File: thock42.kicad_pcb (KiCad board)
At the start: 2 copper layers, 132 x 99.6 mm, 78 parts, among them J1 OLED-128x32, SW1 SW_Push, SW10 SW_Push, SW11 SW_Push, SW12 SW_Push, SW13 SW_Push, SW14 SW_Push, SW15 SW_Push, SW16 SW_Push, SW17 SW_Push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

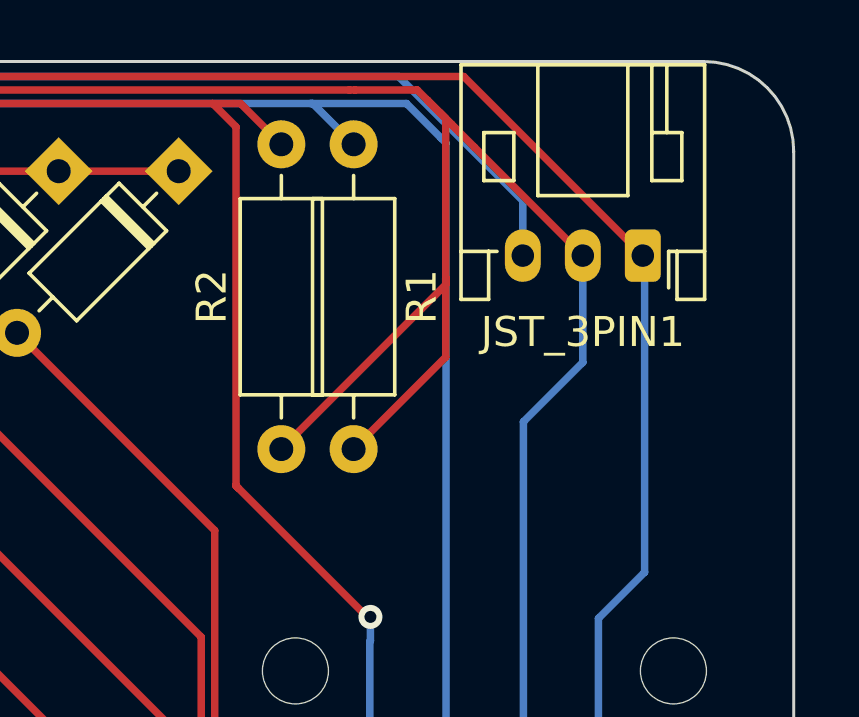
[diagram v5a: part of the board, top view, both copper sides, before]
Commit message: add space between resistors and change some silkscreen labels
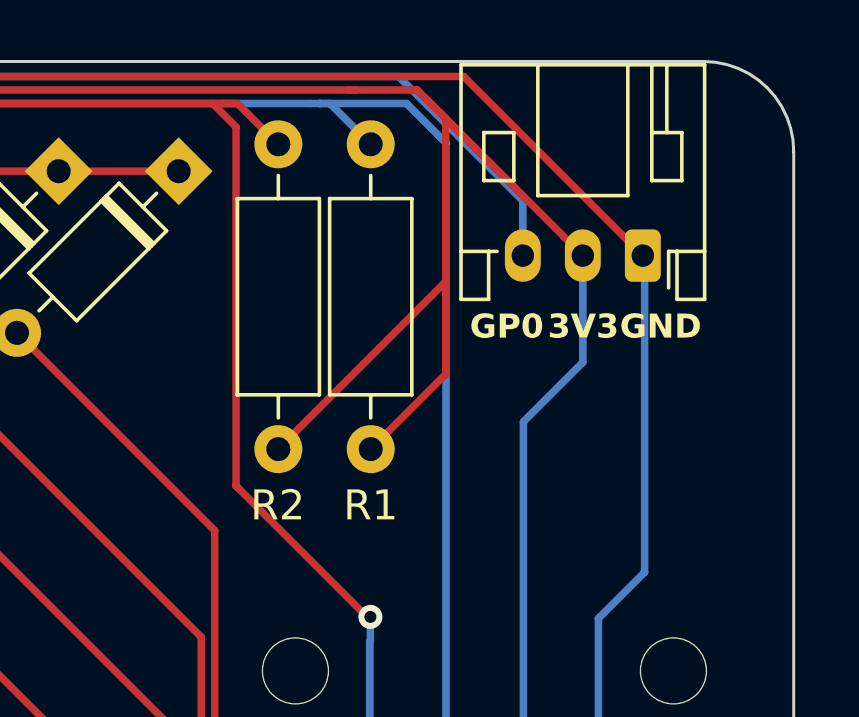
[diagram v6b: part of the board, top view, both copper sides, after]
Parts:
- moved R1 0.57 mm to (203.9, 50.8)
- moved R2 0.10 mm to (200.8, 50.8)
- renumbered JST_3PIN1 to JST_3PIN
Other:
- board text added: "GP0"
- board text removed: "JST_3PIN1"
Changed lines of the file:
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@@
 	(footprint "Resistor_THT:R_Axial_DIN0207_L6.3mm_D2.5mm_P10.16mm_Horizontal"
 		(layer "F.Cu")
-		(at 203.33 50.76 -90)
+		(at 203.9 50.76 -90)
 		(descr "Resistor, Axial_DIN0207 series, Axial, Horizontal, pin pitch=10.16mm, 0.25W = 1/4W, length*diameter=6.3*2.5mm^2, http://cdn-reichelt.de/documents/datenblatt/B400/1_4W%23YAG.pdf")
 		(tags "Resistor Axial_DIN0207 series Axial Horizontal pin pitch 10.16mm 0.25W = 1/4W length 6.3mm diameter 2.5mm")
 		(property "Reference" "R1"
-			(at 5.08 -2.27 -90)
+			(at 12.04 0 0)
 			(layer "F.SilkS")
 			(effects
@@
 		(descr "JST PH series connector, S3B-PH-K (http://www.jst-mfg.com/product/pdf/eng/ePH.pdf), generated with kicad-footprint-generator")
 		(tags "connector JST PH top entry")
-		(property "Reference" "JST_3PIN1"
+		(property "Reference" "JST_3PIN"
 			(at 2 -2.55 180)
 			(layer "F.SilkS")
+			(hide yes)
 			(effects
 				(font
@@
 	(footprint "Resistor_THT:R_Axial_DIN0207_L6.3mm_D2.5mm_P10.16mm_Horizontal"
 		(layer "F.Cu")
-		(at 200.92 50.76 -90)
+		(at 200.82 50.76 -90)
 		(descr "Resistor, Axial_DIN0207 series, Axial, Horizontal, pin pitch=10.16mm, 0.25W = 1/4W, length*diameter=6.3*2.5mm^2, http://cdn-reichelt.de/documents/datenblatt/B400/1_4W%23YAG.pdf")
 		(tags "Resistor Axial_DIN0207 series Axial Horizontal pin pitch 10.16mm 0.25W = 1/4W length 6.3mm diameter 2.5mm")
 		(property "Reference" "R2"
-			(at 5.08 2.32 -90)
+			(at 12.04 0.02 0)
 			(layer "F.SilkS")
 			(effects
@@
 		)
 	)
-	(gr_text "JST_3PIN1"
-		(at 214.83 57.6 -0)
-		(layer "B.SilkS")
-		(effects
-			(font
-				(size 1 1)
-				(thickness 0.15)
-			)
-			(justify left bottom mirror)
-		)
-	)
 	(gr_text "D4"
 		(at 147.8 58.2 45)
@@
 		)
 	)
+	(gr_text "GP0"
+		(at 209.7 57.3 0)
+		(layer "B.SilkS")
+		(effects
+			(font
+				(size 0.8 0.8)
+				(thickness 0.175)
+				(bold yes)
+			)
+			(justify left bottom mirror)
+		)
+	)
 	(gr_text "42"
 		(at 129.91 123 -0)
@@
 		)
 	)
+	(gr_text "GND"
+		(at 214.8 57.3 -0)
+		(layer "B.SilkS")
+		(effects
+			(font
+				(size 0.8 0.8)
+				(thickness 0.175)
+				(bold yes)
+			)
+			(justify left bottom mirror)
+		)
+	)
 	(gr_text "D13"
 		(at 119.6 58.4 45)
@@
 		)
 	)
+	(gr_text "3V3"
+		(at 212.1 57.3 -0)
+		(layer "B.SilkS")
+		(effects
+			(font
+				(size 0.8 0.8)
+				(thickness 0.175)
+				(bold yes)
+			)
+			(justify left bottom mirror)
+		)
+	)
 	(gr_text "D21"
 		(at 191.8 58.2 45)
@@
 		)
 	)
+	(gr_text "3V3"
+		(at 209.8 57.3 0)
+		(layer "F.SilkS")
+		(effects
+			(font
+				(size 0.8 0.8)
+				(thickness 0.175)
+				(bold yes)
+			)
+			(justify left bottom)
+		)
+	)
+	(gr_text "GP0"
+		(at 207.2 57.3 0)
+		(layer "F.SilkS")
+		(effects
+			(font
+				(size 0.8 0.8)
+				(thickness 0.175)
+				(bold yes)
+			)
+			(justify left bottom)
+		)
+	)
 	(gr_text "TH"
 		(at 130.65 125.42 0)
@@
 		)
 	)
+	(gr_text "GND"
+		(at 212.2 57.3 0)
+		(layer "F.SilkS")
+		(effects
+			(font
+				(size 0.8 0.8)
+				(thickness 0.175)
+				(bold yes)
+			)
+			(justify left bottom)
+		)
+	)
 	(gr_text "42"
 		(at 152.66 123 0)
@@
 	)
 	(segment
-		(start 201.97 49.4)
-		(end 201.9 49.4)
-		(width 0.25)
-		(layer "B.Cu")
-		(net 22)
-	)
-	(segment
 		(start 113.874193 50.257017)
 		(end 113.874193 52.325807)
@@
 	)
 	(segment
-		(start 205.093604 49.4)
-		(end 201.9 49.4)
-		(width 0.25)
-		(layer "B.Cu")
-		(net 22)
-	)
-	(segment
-		(start 203.33 50.76)
-		(end 201.97 49.4)
+		(start 202.54 49.4)
+		(end 202.2 49.4)
 		(width 0.25)
 		(layer "B.Cu")
@@
 	)
 	(segment
+		(start 202.2 49.4)
+		(end 201.9 49.4)
+		(width 0.25)
+		(layer "B.Cu")
+		(net 22)
+	)
+	(segment
 		(start 113.874193 52.325807)
 		(end 109.945 56.255)
@@
 	)
 	(segment
+		(start 205.093604 49.4)
+		(end 202.2 49.4)
+		(width 0.25)
+		(layer "B.Cu")
+		(net 22)
+	)
+	(segment
+		(start 203.9 50.76)
+		(end 202.54 49.4)
+		(width 0.25)
+		(layer "B.Cu")
+		(net 22)
+	)
+	(segment
 		(start 113.705904 49.4)
 		(end 113.431739 49.674165)
@@
 	)
 	(segment
-		(start 115.7 49.4)
-		(end 114.73121 49.4)
+		(start 198.63 49.4)
+		(end 199 49.4)
 		(width 0.25)
 		(layer "F.Cu")
@@
 	)
 	(segment
-		(start 199.56 49.4)
-		(end 199.32 49.4)
+		(start 115.7 49.4)
+		(end 114.73121 49.4)
 		(width 0.25)
 		(layer "F.Cu")
@@
 	)
 	(segment
+		(start 199 49.4)
+		(end 199.32 49.4)
+		(width 0.25)
+		(layer "F.Cu")
+		(net 23)
+	)
+	(segment
 		(start 211.49 107.162604)
 		(end 205.19 100.862604)
@@
 	)
 	(segment
-		(start 198.63 49.4)
-		(end 199.32 49.4)
+		(start 200.82 50.76)
+		(end 199.46 49.4)
 		(width 0.25)
 		(layer "F.Cu")
@@
 	)
 	(segment
-		(start 205.19 100.862604)
-		(end 205.19 100.813604)
+		(start 199.46 49.4)
+		(end 199 49.4)
 		(width 0.25)
 		(layer "F.Cu")
@@
 	)
 	(segment
-		(start 200.92 50.76)
-		(end 199.56 49.4)
+		(start 205.19 100.862604)
+		(end 205.19 100.813604)
 		(width 0.25)
 		(layer "F.Cu")
@@
 	)
 	(segment
-		(start 200.92 60.92)
-		(end 206.4 55.44)
-		(width 0.25)
-		(layer "F.Cu")
-		(net 25)
-	)
-	(segment
-		(start 206.4 57.85)
-		(end 206.4 55.2)
-		(width 0.25)
-		(layer "F.Cu")
-		(net 25)
-	)
-	(segment
 		(start 207.245091 106.327513)
 		(end 209.723909 106.327513)
@@
 	)
 	(segment
-		(start 203.33 60.92)
-		(end 206.4 57.85)
+		(start 201.49 108.113604)
+		(end 201.49 94.513604)
 		(width 0.25)
 		(layer "F.Cu")
@@
 	)
 	(segment
-		(start 206.4 49.9)
-		(end 205.8 49.3)
+		(start 104.231 53.715)
+		(end 103.176 54.77)
 		(width 0.25)
 		(layer "F.Cu")
@@
 	)
 	(segment
-		(start 201.49 108.113604)
-		(end 201.49 94.513604)
+		(start 206.4 54.8)
+		(end 206.4 49.9)
 		(width 0.25)
 		(layer "F.Cu")
@@
 	)
 	(segment
-		(start 104.231 53.715)
-		(end 103.176 54.77)
+		(start 206.4 49.9)
+		(end 205.8 49.3)
 		(width 0.25)
 		(layer "F.Cu")
@@
 	)
 	(segment
+		(start 206.4 58.42)
+		(end 206.4 54.8)
+		(width 0.25)
+		(layer "F.Cu")
+		(net 25)
+	)
+	(segment
 		(start 205.8 49.3)
 		(end 205.45 48.95)
@@
 	)
 	(segment
-		(start 206.4 55.2)
-		(end 206.4 49.9)
-		(width 0.25)
-		(layer "F.Cu")
-		(net 25)
-	)
-	(segment
 		(start 203.19 48.95)
 		(end 110.186396 48.95)
@@
 	)
 	(segment
-		(start 206.4 55.44)
-		(end 206.4 55.2)
+		(start 205.45 48.95)
+		(end 203.38 48.95)
 		(width 0.25)
 		(layer "F.Cu")
@@
 	)
 	(segment
-		(start 205.45 48.95)
-		(end 203.38 48.95)
+		(start 200.82 60.92)
+		(end 206.4 55.34)
 		(width 0.25)
 		(layer "F.Cu")
@@
 	)
 	(segment
+		(start 203.9 60.92)
+		(end 206.4 58.42)
+		(width 0.25)
+		(layer "F.Cu")
+		(net 25)
+	)
+	(segment
 		(start 202.59 110.513604)
 		(end 201.49 109.413604)
@@
 		(width 0.25)
 		(layer "F.Cu")
+		(net 25)
+	)
+	(segment
+		(start 206.4 55.34)
+		(end 206.4 54.8)
+		(width 0.25)
+		(layer "F.Cu")

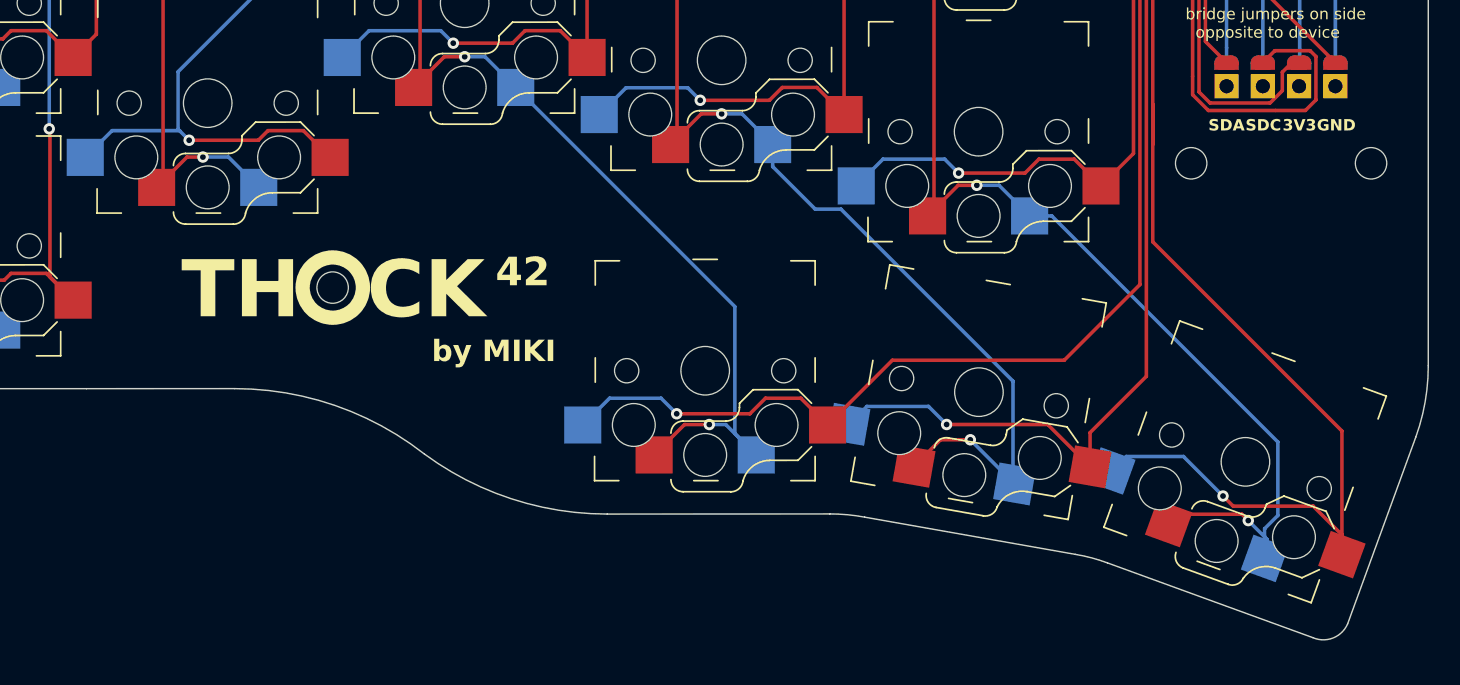
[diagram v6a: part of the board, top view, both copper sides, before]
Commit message: moev thumb cluster down by .2mm
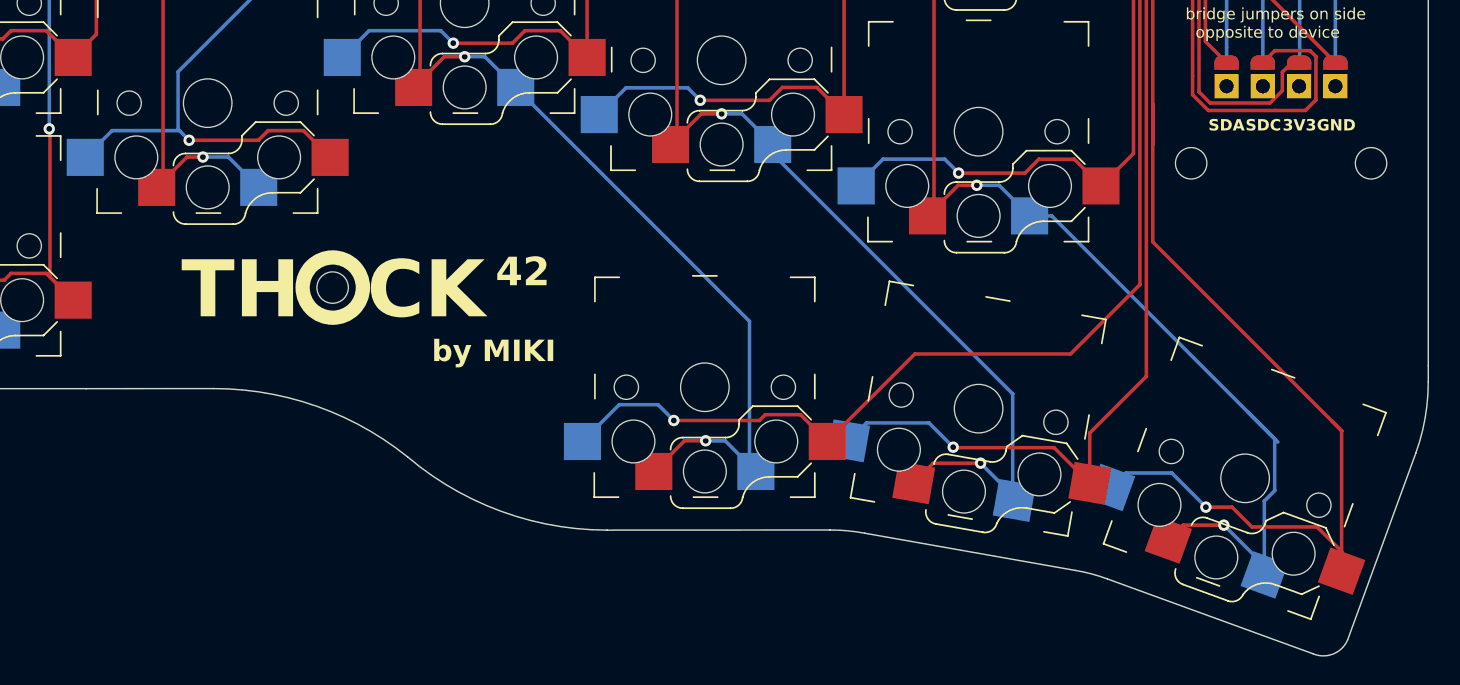
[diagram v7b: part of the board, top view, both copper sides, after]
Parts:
- moved SW19 1.16 mm to (167.3, 129.9)
- moved SW20 1.16 mm to (186.5, 131.4)
- moved SW21 1.16 mm to (205.2, 136.3)
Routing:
- net COL5: track 208.4 -> 212.0 mm
- net Net-(D21-A): track 115.8 -> 118.0 mm
- net Net-(D20-A): track 103.4 -> 104.6 mm
- net COL3: track 157.1 -> 158.2 mm
- net Net-(D19-A): track 116.9 -> 117.4 mm
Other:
- board size 132 x 99.6 mm -> 132 x 100.7 mm

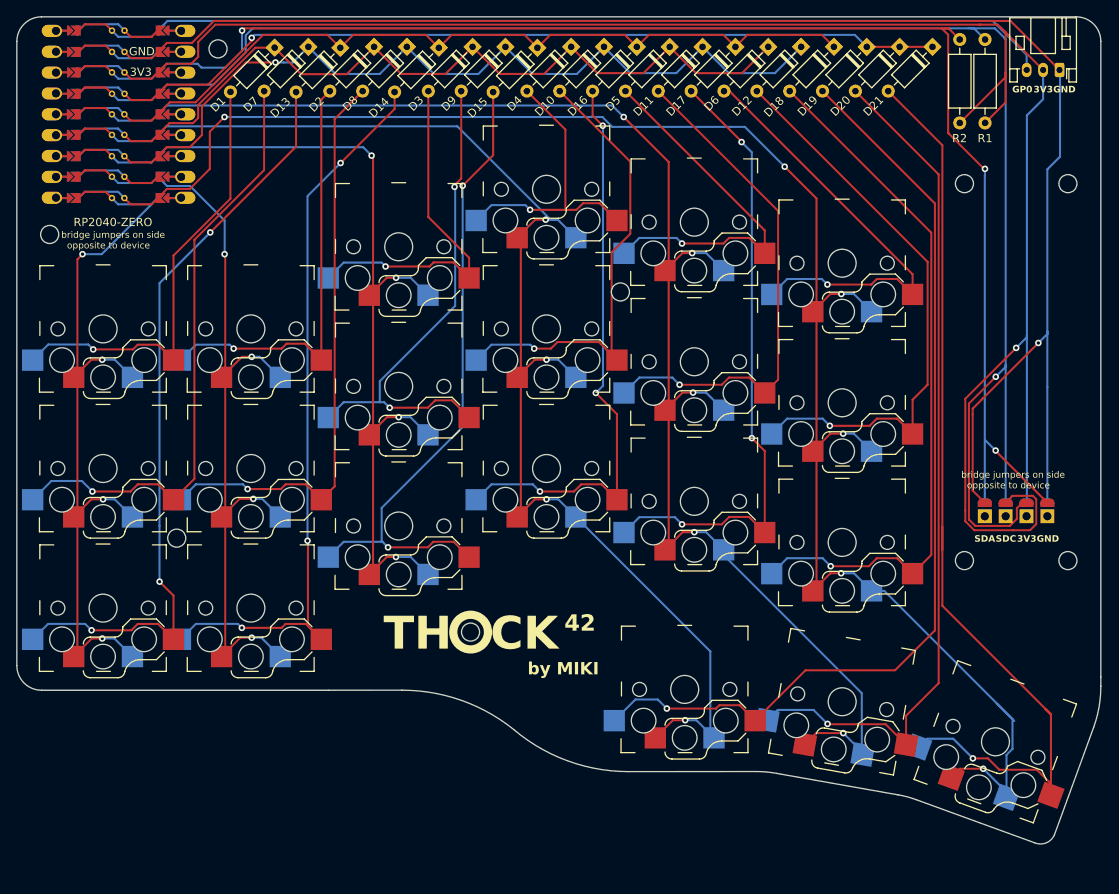
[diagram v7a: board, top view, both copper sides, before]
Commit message: adapt to symmetric keycap spacing
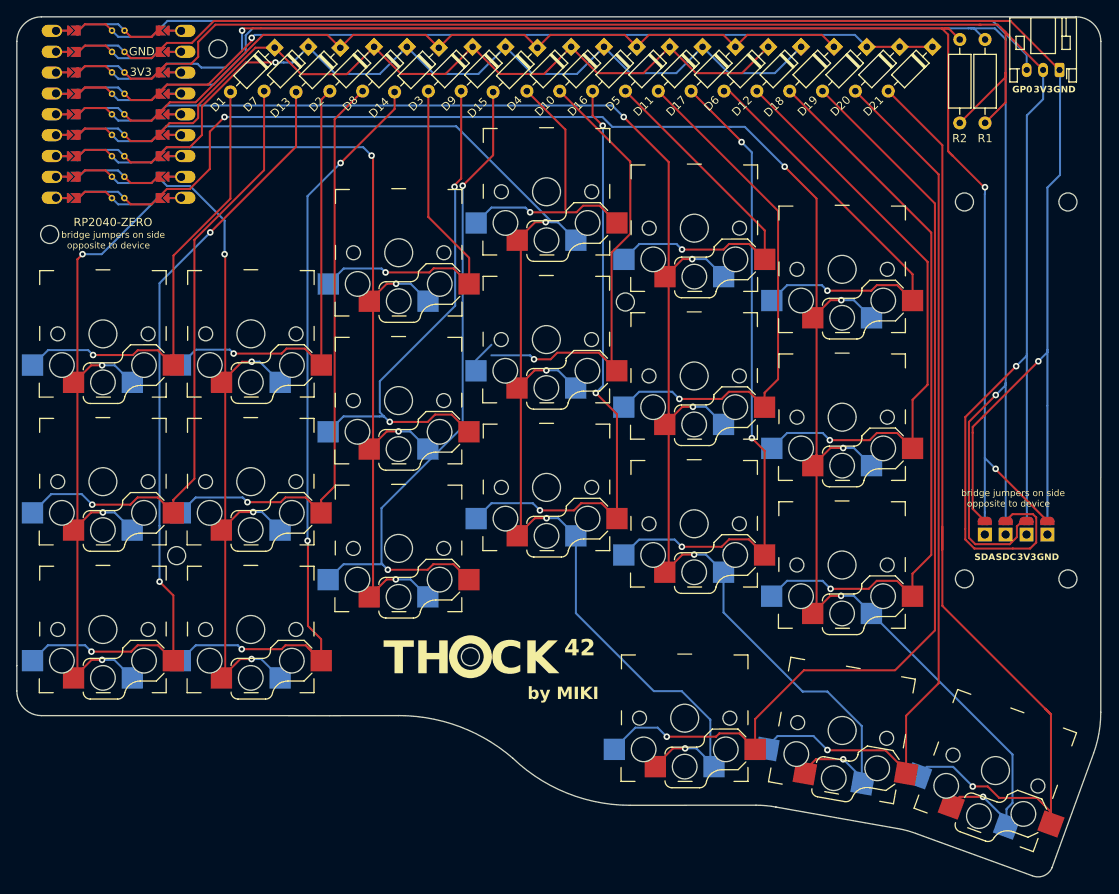
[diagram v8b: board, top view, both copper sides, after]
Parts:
- moved SW19 3.50 mm to (167.3, 133.4)
- moved SW20 3.50 mm to (186.5, 134.9)
- moved SW21 3.50 mm to (205.2, 139.8)
- moved REF** 3.00 mm to (141.2, 125.9)
- moved SW18 2.75 mm to (186.5, 114.8)
- moved SW15 2.73 mm to (132.5, 112.7)
- moved SW17 2.73 mm to (168.5, 109.7)
- moved SW13 2.60 mm to (96.5, 122.6)
- moved SW14 2.60 mm to (114.5, 122.6)
- moved SW16 2.30 mm to (150.5, 105.3)
- moved REF** 2.23 mm to (201.4, 70.5)
- moved REF** 2.23 mm to (214.0, 70.5)
- moved J1 2.23 mm to (201.7, 112.6)
- moved REF** 2.23 mm to (214.0, 116.4)
- moved REF** 2.23 mm to (201.4, 116.4)
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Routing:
- net COL4: track 181.2 -> 188.3 mm
- net COL3: track 158.2 -> 164.5 mm
- net Net-(D14-A): track 90.8 -> 95.7 mm
- net COL2: track 105.7 -> 109.6 mm
- net Net-(D19-A): track 117.4 -> 121.0 mm
- net COL1: track 91.7 -> 95.2 mm
- net COL0: track 89.0 -> 92.6 mm
- net Net-(D21-A): track 118.0 -> 121.4 mm
- net Net-(D20-A): track 104.6 -> 108.0 mm
- net OLED_SDA: track 173.5 -> 176.3 mm
- net Net-(D18-A): track 86.3 -> 89.1 mm
- net Net-(D15-A): track 79.7 -> 82.4 mm
- net Net-(D17-A): track 76.9 -> 79.6 mm
- net Net-(D13-A): track 93.6 -> 96.2 mm
- net Net-(D16-A): track 71.1 -> 73.4 mm
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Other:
- board size 132 x 100.7 mm -> 132 x 104.7 mm
